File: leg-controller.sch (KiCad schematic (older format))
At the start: 24 parts

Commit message: Added values to some components
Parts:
- removed U?: ATmega328P-PU, Package_DIP:DIP-28_W7.62mm, symbol MCU_Microchip_ATmega:ATmega328P-PU
- added U?: ATmega328P-PU, Package_DIP:DIP-28_W7.62mm, symbol MCU_Microchip_ATmega:ATmega328P-PU
- C?: value C -> 100n
- C? (x2): value C -> 22p
- Y?: value Crystal -> 16MHz
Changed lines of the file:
@@
 	7050 1800 7150 1800
-$Comp
-L MCU_Microchip_ATmega:ATmega328P-PU U?
-U 1 1 618BE8FD
-P 4550 4700
-F 0 "U?" H 3906 4746 50  0000 R CNN
-F 1 "ATmega328P-PU" H 3906 4655 50  0000 R CNN
-F 2 "Package_DIP:DIP-28_W7.62mm" H 4550 4700 50  0001 C CIN
-F 3 "http://ww1.microchip.com/downloads/en/DeviceDoc/ATmega328_P%20AVR%20MCU%20with%20picoPower%20Technology%20Data%20Sheet%2040001984A.pdf" H 4550 4700 50  0001 C CNN
-	1    4550 4700
-	1    0    0    -1
-$EndComp
 $Comp
 L power:+3.3V #PWR?
@@
 P 3850 6400
 F 0 "C?" H 3965 6446 50  0000 L CNN
-F 1 "C" H 3965 6355 50  0000 L CNN
+F 1 "100n" H 3965 6355 50  0000 L CNN
 F 2 "" H 3888 6250 50  0001 C CNN
 F 3 "~" H 3850 6400 50  0001 C CNN
@@
 P 5550 6150
 F 0 "Y?" H 5550 5882 50  0000 C CNN
-F 1 "Crystal" H 5550 5973 50  0000 C CNN
+F 1 "16MHz" H 5550 5973 50  0000 C CNN
 F 2 "" H 5550 6150 50  0001 C CNN
 F 3 "~" H 5550 6150 50  0001 C CNN
@@
 P 5350 6400
 F 0 "C?" H 5465 6446 50  0000 L CNN
-F 1 "C" H 5465 6355 50  0000 L CNN
+F 1 "22p" H 5465 6355 50  0000 L CNN
 F 2 "" H 5388 6250 50  0001 C CNN
 F 3 "~" H 5350 6400 50  0001 C CNN
@@
 P 5750 6400
 F 0 "C?" H 5865 6446 50  0000 L CNN
-F 1 "C" H 5865 6355 50  0000 L CNN
+F 1 "22p" H 5865 6355 50  0000 L CNN
 F 2 "" H 5788 6250 50  0001 C CNN
 F 3 "~" H 5750 6400 50  0001 C CNN
@@
 Wire Wire Line
 	5900 4600 5150 4600
+$Comp
+L MCU_Microchip_ATmega:ATmega328P-PU U?
+U 1 1 617FB84E
+P 4550 4700
+F 0 "U?" H 3906 4746 50  0000 R CNN
+F 1 "ATmega328P-PU" H 3906 4655 50  0000 R CNN
+F 2 "Package_DIP:DIP-28_W7.62mm" H 4550 4700 50  0001 C CIN
+F 3 "http://ww1.microchip.com/downloads/en/DeviceDoc/ATmega328_P%20AVR%20MCU%20with%20picoPower%20Technology%20Data%20Sheet%2040001984A.pdf" H 4550 4700 50  0001 C CNN
+	1    4550 4700
+	1    0    0    -1
+$EndComp
 $EndSCHEMATC

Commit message: Various changes.
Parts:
- removed C?: C, symbol Device:C
- removed D?: D_Zener, symbol Device:D_Zener
- removed J? (x2): Conn_01x03, symbol Connector_Generic:Conn_01x03
- removed J?: Conn_02x01, symbol Connector_Generic:Conn_02x01
- removed Q?: Q_NPN_BCE, symbol Device:Q_NPN_BCE
- removed Q?: Q_PMOS_DGS, symbol Device:Q_PMOS_DGS
- removed R? (x9): R, symbol Device:R
- removed U?: Opamp_Quad_Generic, symbol Device:Opamp_Quad_Generic
- removed U?: ATmega328P-PU, Package_DIP:DIP-28_W7.62mm, symbol MCU_Microchip_ATmega:ATmega328P-PU
- added C1: 470u, symbol Device:C
- added C? (x2): CP, symbol Device:CP
- added J1: Conn_01x02, symbol Connector_Generic:Conn_01x02
- added R1: 0, symbol Device:R
- added U1: ATmega644P-20AU, Package_QFP:TQFP-44_10x10mm_P0.8mm, symbol MCU_Microchip_ATmega:ATmega644P-20AU
- added U?: LD1117S33TR_SOT223, Package_TO_SOT_SMD:SOT-223-3_TabPin2, symbol Regulator_Linear:LD1117S33TR_SOT223
- Y1: renamed from Y?; value 16MHz -> 12MHz
- gave numbers to parts that had none: 5
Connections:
- net labels added: I2C_SCL, I2C_SDA, ROT_CLK_A, ROT_CLK_B, ROT_CLK_C, ROT_DAT_A, ROT_DAT_B, ROT_DAT_C, SPI_MISO, SPI_MOSI, SPI_SCK
- net labels removed: +BATT, MOTOR_A_DISCONNECT, SCL, SDA
- wire segments 80 -> 68
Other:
- moved on the sheet: C2, C3, C4, Y1

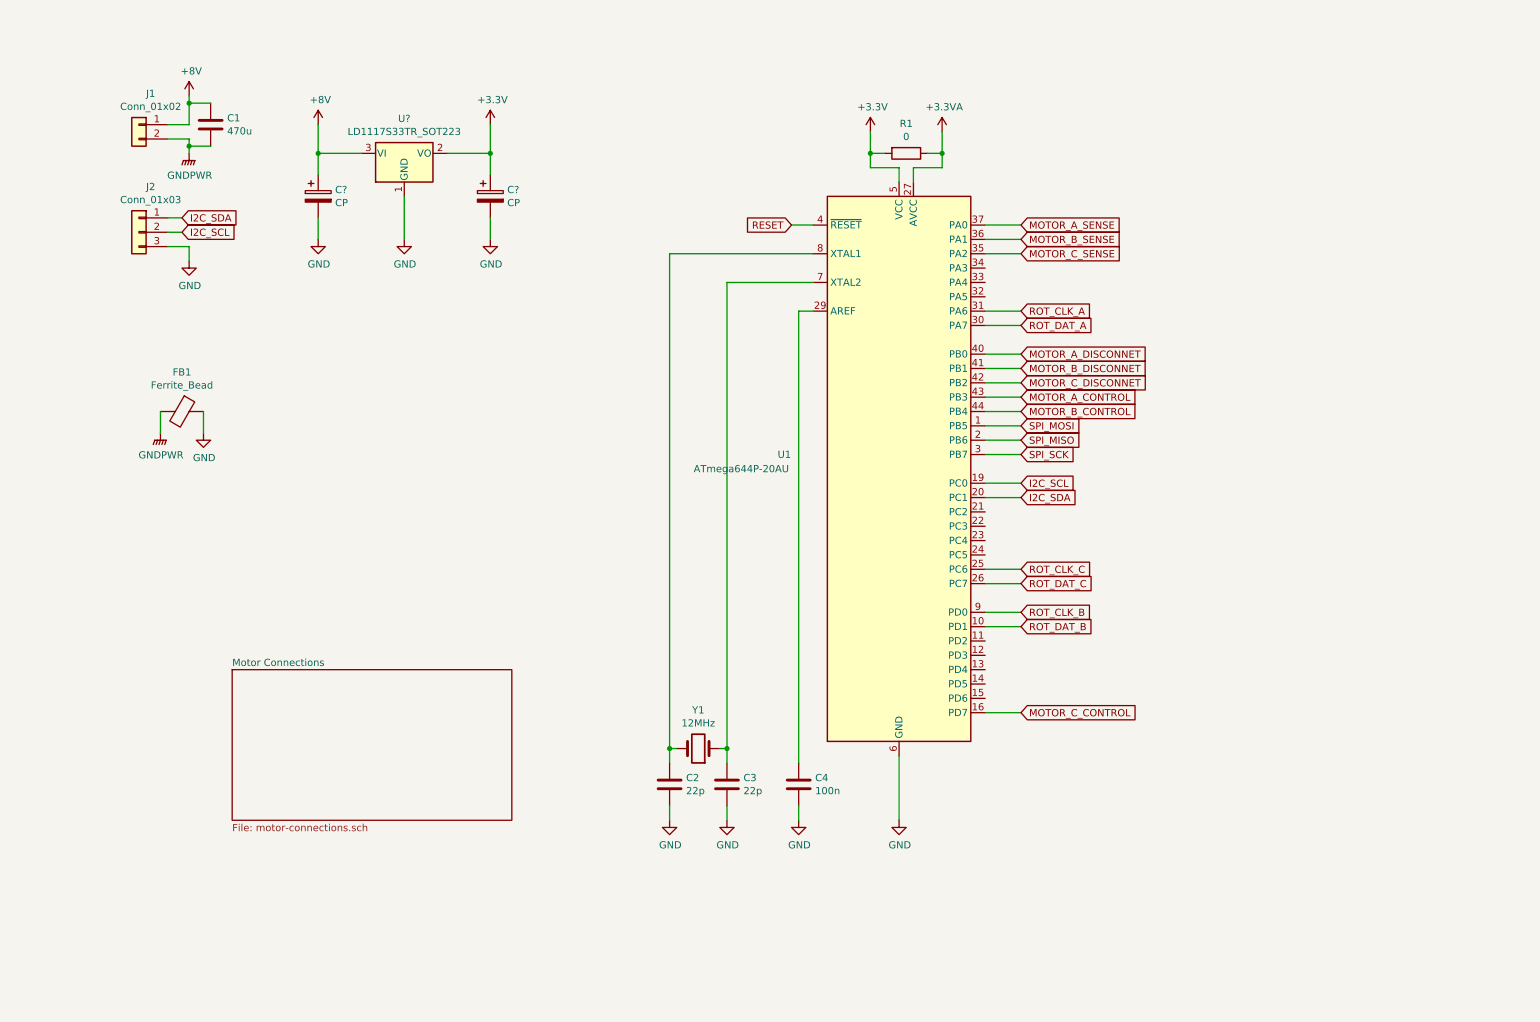
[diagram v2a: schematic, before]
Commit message: Fixed amplifier circuit and did some rearranging
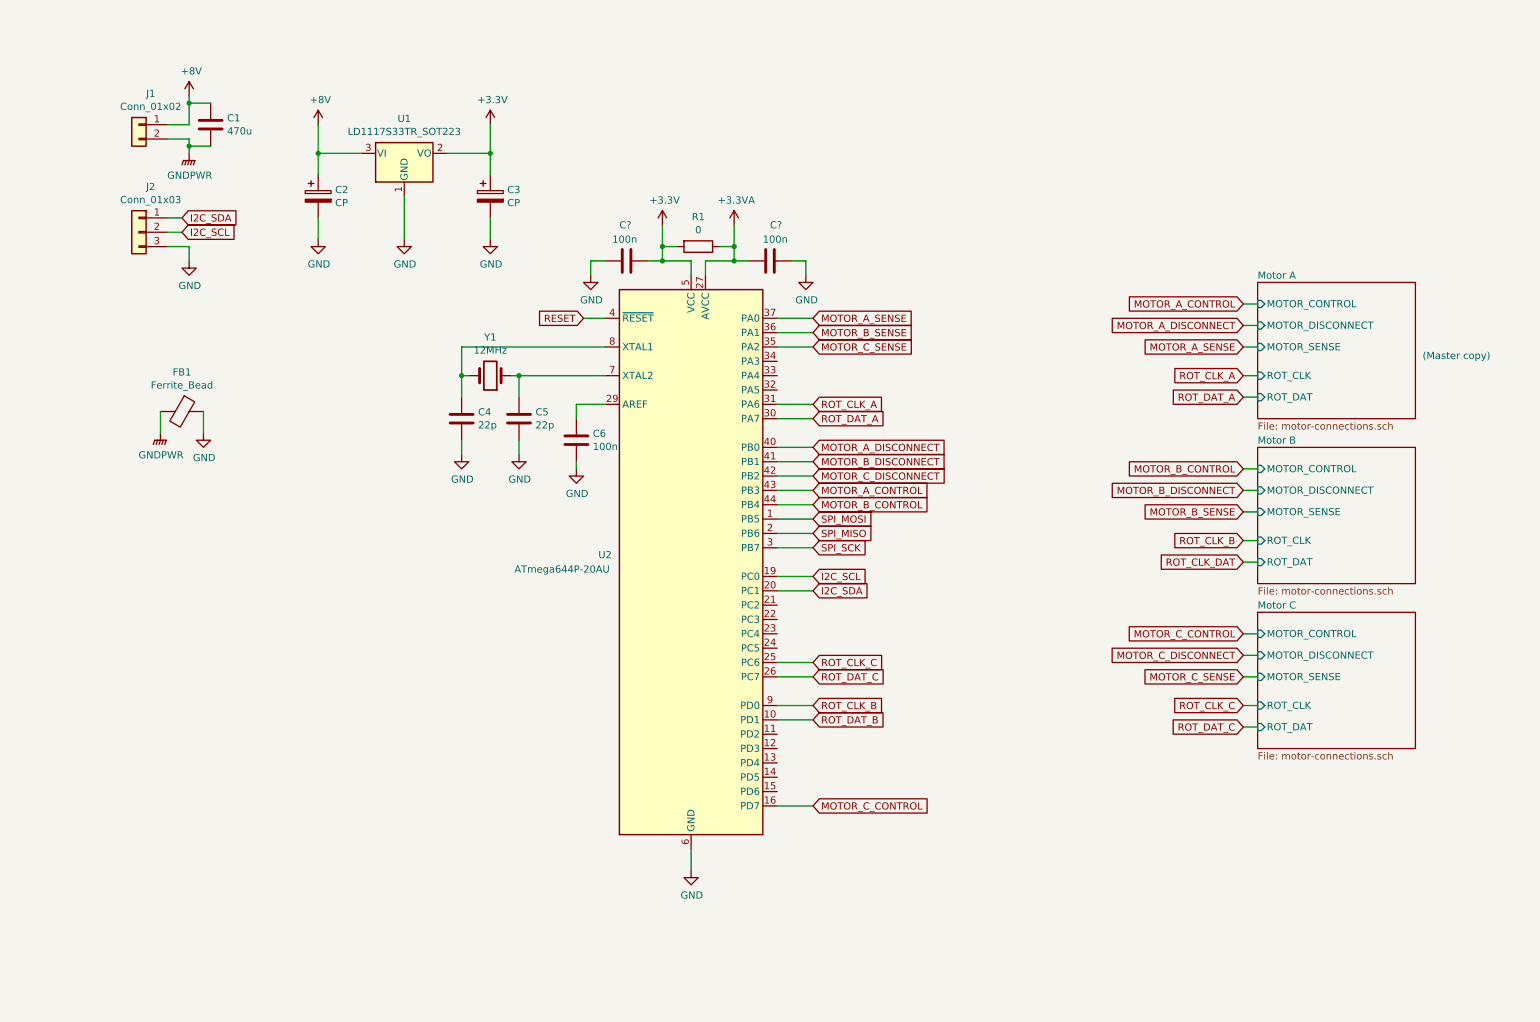
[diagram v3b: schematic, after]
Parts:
- added C? (x2): 100n, symbol Device:C
- gave numbers to parts that had none: 3
- renumbered C2 to C4, C3 to C5, C4 to C6, U1 to U2
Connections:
- net +3.3VA: now also C?.2
- net +3V3: now also C?.1
- net GND: now also C?.1, C?.2
- net MOTOR_A_DISCONNET renamed MOTOR_A_DISCONNECT
- net MOTOR_B_DISCONNET renamed MOTOR_B_DISCONNECT
- net MOTOR_C_DISCONNET renamed MOTOR_C_DISCONNECT
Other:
- note added: "(Master copy)"
- moved on the sheet: C4, C5, C6, R1, U2, Y1

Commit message: Various changes
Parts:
- added D?: LED_RUN, symbol Device:LED
- added D?: LED_POWER, symbol Device:LED
- added D?: LED_3V3, symbol Device:LED
- added D?: LED_ERR, symbol Device:LED
- added D?: D, symbol Device:D
- added J?: Motor_D, symbol Connector_Generic:Conn_01x05
- added J?: Motor_F, symbol Connector_Generic:Conn_01x05
- added J?: Motor_E, symbol Connector_Generic:Conn_01x05
- added J?: ISP, symbol Connector_Generic:Conn_02x03_Odd_Even
- added J?: UART, symbol Connector_Generic:Conn_01x04
- added J?: General_Pins, symbol Connector_Generic:Conn_01x04
- added J?: USB_B_Mini, symbol Connector:USB_B_Mini
- added R? (x4): R, symbol Device:R
- added R? (x2): 68, symbol Device:R
- added R?: 1.5k, symbol Device:R
- J1: value Conn_01x02 -> Power
- J2: value Conn_01x03 -> I2C
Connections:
- net +3V3: now also J?.1 (Pin_1), J?.2 (Pin_2), R?.1, R?.1
- net +8V: now also D?.1 (K), R?.1
- net GND: now also D?.1 (K), D?.1 (K), D?.1 (K), D?.1 (K), J?.4 (Pin_4), J?.4 (Pin_4), J?.5 (GND), J?.5 (Pin_5), J?.5 (Pin_5), J?.5 (Pin_5), J?.6 (Pin_6)
- net MOTOR_A_CONTROL: now also U2.44 (PB4); no longer U2.43 (PB3)
- net MOTOR_A_DISCONNECT: now also U2.21 (PC2); no longer U2.40 (PB0)
- net MOTOR_B_CONTROL: now also U2.15 (PD6); no longer U2.44 (PB4)
- net MOTOR_B_DISCONNECT: now also U2.22 (PC3); no longer U2.41 (PB1)
- net MOTOR_C_DISCONNECT: now also U2.23 (PC4); no longer U2.42 (PB2)
- net RESET: now also J?.5 (Pin_5)
- net SPI_MISO: now also J?.1 (Pin_1), J?.2 (Pin_2), J?.2 (Pin_2), J?.2 (Pin_2)
- net SPI_MOSI: now also J?.1 (Pin_1), J?.1 (Pin_1), J?.1 (Pin_1), J?.4 (Pin_4)
- net SPI_SCK: now also J?.3 (Pin_3), J?.3 (Pin_3), J?.3 (Pin_3), J?.3 (Pin_3)
- net UART_RXD: now reaches U2.11 (PD2)
- net UART_RXD: now also J?.3 (Pin_3)
- net UART_TXD: now reaches U2.12 (PD3)
- net UART_TXD: now also J?.2 (Pin_2)
- net SPI_SS_E: now reaches U2.13 (PD4)
- net SPI_SS_E: now also J?.4 (Pin_4)
- net SPI_SS_F: now reaches U2.14 (PD5)
- net SPI_SS_F: now also J?.4 (Pin_4)
- net SPI_SS_D: now reaches U2.24 (PC5)
- net SPI_SS_D: now also J?.4 (Pin_4)
- net GENERAL_C: now reaches U2.32 (PA5)
- net GENERAL_C: now also J?.3 (Pin_3)
- net GENERAL_B: now reaches U2.33 (PA4)
- net GENERAL_B: now also J?.2 (Pin_2)
- net GENERAL_A: now reaches U2.34 (PA3)
- net GENERAL_A: now also J?.1 (Pin_1)
- new net: D?.2 (A), R?.2 (x4)
- new net: J?.2 (D-), R?.1, R?.2
- new net: J?.3 (D+), R?.2
- new net +5V: D?.2 (A), J?.1 (VBUS)
- new net LED_ERR: R?.1, U2.41 (PB1)
- new net LED_RUN: R?.1, U2.40 (PB0)
- new net USB_D+: R?.1, U2.42 (PB2)
- new net USB_D-: R?.2, U2.43 (PB3)
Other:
- moved on the sheet: C1, C2, C3, C4, C5, C6, C?, FB1, J1, J2, R1, U1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

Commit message: Various changes.
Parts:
- removed J?: General_Pins, symbol Connector_Generic:Conn_01x04
- added SW?: Function, symbol Switch:SW_DIP_x04
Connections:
- net GND: now also SW?.5, SW?.6, SW?.7, SW?.8
- net GENERAL_A renamed FUNCTION_0
- net FUNCTION_0: now also SW?.1
- net GENERAL_B renamed FUNCTION_1
- net FUNCTION_1: now also SW?.2
- net GENERAL_C renamed FUNCTION_2
- net FUNCTION_2: now also SW?.3
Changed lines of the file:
@@
 Wire Wire Line
 	3150 3250 3250 3250
-Text GLabel 1150 4050 2    50   Input ~ 0
-GENERAL_A
-Text GLabel 1150 4150 2    50   Input ~ 0
-GENERAL_B
-Text GLabel 1150 4250 2    50   Input ~ 0
-GENERAL_C
-Wire Wire Line
-	1150 4050 1050 4050
-Wire Wire Line
-	1050 4150 1150 4150
-Wire Wire Line
-	1150 4250 1050 4250
-$Comp
-L power:GND #PWR?
-U 1 1 61C68C47
-P 1150 4450
-F 0 "#PWR?" H 1150 4200 50  0001 C CNN
-F 1 "GND" H 1155 4277 50  0000 C CNN
-F 2 "" H 1150 4450 50  0001 C CNN
-F 3 "" H 1150 4450 50  0001 C CNN
-	1    1150 4450
-	-1   0    0    -1
-$EndComp
-Wire Wire Line
-	1150 4450 1150 4350
-Wire Wire Line
-	1150 4350 1050 4350
 $Comp
 L power:+5V #PWR?
@@
 $Comp
 L Connector_Generic:Conn_01x04 J?
-U 1 1 61C5169E
-P 850 4150
-F 0 "J?" H 768 4467 50  0000 C CNN
-F 1 "General_Pins" H 768 4376 50  0000 C CNN
-F 2 "" H 850 4150 50  0001 C CNN
-F 3 "~" H 850 4150 50  0001 C CNN
-	1    850  4150
-	-1   0    0    -1
-$EndComp
-$Comp
-L power:GND #PWR04
-U 1 1 6179673C
-P 1200 5300
-F 0 "#PWR04" H 1200 5050 50  0001 C CNN
-F 1 "GND" H 1205 5127 50  0000 C CNN
-F 2 "" H 1200 5300 50  0001 C CNN
-F 3 "" H 1200 5300 50  0001 C CNN
-	1    1200 5300
-	1    0    0    -1
-$EndComp
-Wire Wire Line
-	1200 5200 1200 5300
-Wire Wire Line
-	1050 5200 1200 5200
-Wire Wire Line
-	1050 5000 1150 5000
-Wire Wire Line
-	1050 5100 1150 5100
-Text GLabel 1150 5000 2    50   Input ~ 0
-I2C_SDA
-Text GLabel 1150 5100 2    50   Input ~ 0
-I2C_SCL
-$Comp
-L Connector_Generic:Conn_01x03 J2
-U 1 1 61793AA3
-P 850 5100
-F 0 "J2" H 768 5417 50  0000 C CNN
-F 1 "I2C" H 768 5326 50  0000 C CNN
-F 2 "" H 850 5100 50  0001 C CNN
-F 3 "~" H 850 5100 50  0001 C CNN
-	1    850  5100
-	-1   0    0    -1
-$EndComp
-$Comp
-L Connector_Generic:Conn_01x04 J?
 U 1 1 61B3D105
 P 850 3200
@@
 Wire Wire Line
 	1050 3200 1150 3200
-$Comp
-L Connector:USB_B_Mini J?
-U 1 1 61C85C74
-P 2450 4800
-F 0 "J?" H 2507 5267 50  0000 C CNN
-F 1 "USB_B_Mini" H 2507 5176 50  0000 C CNN
-F 2 "" H 2600 4750 50  0001 C CNN
-F 3 "~" H 2600 4750 50  0001 C CNN
-	1    2450 4800
-	1    0    0    -1
-$EndComp
-$Comp
-L Device:R R?
-U 1 1 61C9C39E
-P 3350 4800
-F 0 "R?" V 3143 4800 50  0000 C CNN
-F 1 "68" V 3234 4800 50  0000 C CNN
-F 2 "" V 3280 4800 50  0001 C CNN
-F 3 "~" H 3350 4800 50  0001 C CNN
-	1    3350 4800
-	0    1    1    0
-$EndComp
-$Comp
-L Device:R R?
-U 1 1 61C9D08A
-P 3350 4900
-F 0 "R?" V 3250 4900 50  0000 C CNN
-F 1 "68" V 3150 4900 50  0000 C CNN
-F 2 "" V 3280 4900 50  0001 C CNN
-F 3 "~" H 3350 4900 50  0001 C CNN
-	1    3350 4900
-	0    -1   -1   0
-$EndComp
-$Comp
-L Device:R R?
-U 1 1 61CB53AC
-P 3100 4400
-F 0 "R?" H 3170 4446 50  0000 L CNN
-F 1 "1.5k" H 3170 4355 50  0000 L CNN
-F 2 "" V 3030 4400 50  0001 C CNN
-F 3 "~" H 3100 4400 50  0001 C CNN
-	1    3100 4400
-	1    0    0    -1
-$EndComp
-Wire Wire Line
-	3100 4550 3100 4900
-Connection ~ 3100 4900
-Wire Wire Line
-	3100 4900 3200 4900
-$Comp
-L power:+3.3V #PWR?
-U 1 1 61CBCED0
-P 3100 4150
-F 0 "#PWR?" H 3100 4000 50  0001 C CNN
-F 1 "+3.3V" H 3115 4323 50  0000 C CNN
-F 2 "" H 3100 4150 50  0001 C CNN
-F 3 "" H 3100 4150 50  0001 C CNN
-	1    3100 4150
-	1    0    0    -1
-$EndComp
-Wire Wire Line
-	3100 4150 3100 4250
-$Comp
-L power:GND #PWR?
-U 1 1 61CC49B7
-P 2450 5300
-F 0 "#PWR?" H 2450 5050 50  0001 C CNN
-F 1 "GND" H 2455 5127 50  0000 C CNN
-F 2 "" H 2450 5300 50  0001 C CNN
-F 3 "" H 2450 5300 50  0001 C CNN
-	1    2450 5300
-	1    0    0    -1
-$EndComp
-Wire Wire Line
-	2450 5200 2450 5300
-Wire Wire Line
-	3600 4800 3500 4800
-Wire Wire Line
-	3500 4900 3600 4900
-$Comp
-L power:+5V #PWR?
-U 1 1 61D1E6C0
-P 2850 4150
-F 0 "#PWR?" H 2850 4000 50  0001 C CNN
-F 1 "+5V" H 2865 4323 50  0000 C CNN
-F 2 "" H 2850 4150 50  0001 C CNN
-F 3 "" H 2850 4150 50  0001 C CNN
-	1    2850 4150
-	1    0    0    -1
-$EndComp
-Wire Wire Line
-	2750 4600 2850 4600
-Wire Wire Line
-	2850 4600 2850 4150
-Wire Wire Line
-	2750 4800 3200 4800
-Wire Wire Line
-	2750 4900 3100 4900
 Wire Wire Line
 	3550 6200 3450 6200
@@
 	6500 5200 6750 5200
 Text GLabel 6750 2600 2    50   Input ~ 0
-GENERAL_A
+FUNCTION_0
 Text GLabel 6750 2700 2    50   Input ~ 0
-GENERAL_B
+FUNCTION_1
 Text GLabel 6750 2800 2    50   Input ~ 0
-GENERAL_C
+FUNCTION_2
 Wire Wire Line
 	6750 2600 6500 2600
@@
 Wire Wire Line
 	4700 2700 5300 2700
+Text GLabel 3600 4800 2    50   Input ~ 0
+USB_D+
 Text GLabel 3600 4900 2    50   Input ~ 0
 USB_D-
-Text GLabel 3600 4800 2    50   Input ~ 0
-USB_D+
+Wire Wire Line
+	2750 4900 3100 4900
+Wire Wire Line
+	2750 4800 3200 4800
+Wire Wire Line
+	2850 4600 2850 4150
+Wire Wire Line
+	2750 4600 2850 4600
+$Comp
+L power:+5V #PWR?
+U 1 1 61D1E6C0
+P 2850 4150
+F 0 "#PWR?" H 2850 4000 50  0001 C CNN
+F 1 "+5V" H 2865 4323 50  0000 C CNN
+F 2 "" H 2850 4150 50  0001 C CNN
+F 3 "" H 2850 4150 50  0001 C CNN
+	1    2850 4150
+	1    0    0    -1
+$EndComp
+Wire Wire Line
+	3500 4900 3600 4900
+Wire Wire Line
+	3600 4800 3500 4800
+Wire Wire Line
+	2450 5200 2450 5300
+$Comp
+L power:GND #PWR?
+U 1 1 61CC49B7
+P 2450 5300
+F 0 "#PWR?" H 2450 5050 50  0001 C CNN
+F 1 "GND" H 2455 5127 50  0000 C CNN
+F 2 "" H 2450 5300 50  0001 C CNN
+F 3 "" H 2450 5300 50  0001 C CNN
+	1    2450 5300
+	1    0    0    -1
+$EndComp
+Wire Wire Line
+	3100 4150 3100 4250
+$Comp
+L power:+3.3V #PWR?
+U 1 1 61CBCED0
+P 3100 4150
+F 0 "#PWR?" H 3100 4000 50  0001 C CNN
+F 1 "+3.3V" H 3115 4323 50  0000 C CNN
+F 2 "" H 3100 4150 50  0001 C CNN
+F 3 "" H 3100 4150 50  0001 C CNN
+	1    3100 4150
+	1    0    0    -1
+$EndComp
+Wire Wire Line
+	3100 4900 3200 4900
+Connection ~ 3100 4900
+Wire Wire Line
+	3100 4550 3100 4900
+$Comp
+L Device:R R?
+U 1 1 61CB53AC
+P 3100 4400
+F 0 "R?" H 3170 4446 50  0000 L CNN
+F 1 "1.5k" H 3170 4355 50  0000 L CNN
+F 2 "" V 3030 4400 50  0001 C CNN
+F 3 "~" H 3100 4400 50  0001 C CNN
+	1    3100 4400
+	1    0    0    -1
+$EndComp
+$Comp
+L Device:R R?
+U 1 1 61C9D08A
+P 3350 4900
+F 0 "R?" V 3250 4900 50  0000 C CNN
+F 1 "68" V 3150 4900 50  0000 C CNN
+F 2 "" V 3280 4900 50  0001 C CNN
+F 3 "~" H 3350 4900 50  0001 C CNN
+	1    3350 4900
+	0    -1   -1   0
+$EndComp
+$Comp
+L Device:R R?
+U 1 1 61C9C39E
+P 3350 4800
+F 0 "R?" V 3143 4800 50  0000 C CNN
+F 1 "68" V 3234 4800 50  0000 C CNN
+F 2 "" V 3280 4800 50  0001 C CNN
+F 3 "~" H 3350 4800 50  0001 C CNN
+	1    3350 4800
+	0    1    1    0
+$EndComp
+$Comp
+L Connector:USB_B_Mini J?
+U 1 1 61C85C74
+P 2450 4800
+F 0 "J?" H 2507 5267 50  0000 C CNN
+F 1 "USB_B_Mini" H 2507 5176 50  0000 C CNN
+F 2 "" H 2600 4750 50  0001 C CNN
+F 3 "~" H 2600 4750 50  0001 C CNN
+	1    2450 4800
+	1    0    0    -1
+$EndComp
+$Comp
+L Connector_Generic:Conn_01x03 J2
+U 1 1 61793AA3
+P 850 5100
+F 0 "J2" H 768 5417 50  0000 C CNN
+F 1 "I2C" H 768 5326 50  0000 C CNN
+F 2 "" H 850 5100 50  0001 C CNN
+F 3 "~" H 850 5100 50  0001 C CNN
+	1    850  5100
+	-1   0    0    -1
+$EndComp
+Text GLabel 1150 5100 2    50   Input ~ 0
+I2C_SCL
+Text GLabel 1150 5000 2    50   Input ~ 0
+I2C_SDA
+Wire Wire Line
+	1050 5100 1150 5100
+Wire Wire Line
+	1050 5000 1150 5000
+Wire Wire Line
+	1050 5200 1200 5200
+Wire Wire Line
+	1200 5200 1200 5300
+$Comp
+L power:GND #PWR04
+U 1 1 6179673C
+P 1200 5300
+F 0 "#PWR04" H 1200 5050 50  0001 C CNN
+F 1 "GND" H 1205 5127 50  0000 C CNN
+F 2 "" H 1200 5300 50  0001 C CNN
+F 3 "" H 1200 5300 50  0001 C CNN
+	1    1200 5300
+	1    0    0    -1
+$EndComp
+Wire Wire Line
+	1200 4300 1300 4300
+Wire Wire Line
+	1200 4200 1300 4200
+Wire Wire Line
+	1200 4100 1300 4100
+Text GLabel 1200 4300 0    50   Input ~ 0
+FUNCTION_2
+Text GLabel 1200 4200 0    50   Input ~ 0
+FUNCTION_1
+Text GLabel 1200 4100 0    50   Input ~ 0
+FUNCTION_0
+Wire Wire Line
+	2000 4400 2000 4500
+Connection ~ 2000 4400
+Wire Wire Line
+	1900 4400 2000 4400
+Wire Wire Line
+	2000 4300 2000 4400
+Connection ~ 2000 4300
+Wire Wire Line
+	1900 4300 2000 4300
+Wire Wire Line
+	2000 4200 2000 4300
+Connection ~ 2000 4200
+Wire Wire Line
+	1900 4200 2000 4200
+Wire Wire Line
+	2000 4100 2000 4200
+Wire Wire Line
+	1900 4100 2000 4100
+$Comp
+L power:GND #PWR?
+U 1 1 6199B184
+P 2000 4500
+F 0 "#PWR?" H 2000 4250 50  0001 C CNN
+F 1 "GND" H 2005 4327 50  0000 C CNN
+F 2 "" H 2000 4500 50  0001 C CNN
+F 3 "" H 2000 4500 50  0001 C CNN
+	1    2000 4500
+	1    0    0    -1
+$EndComp
+$Comp
+L Switch:SW_DIP_x04 SW?
+U 1 1 6199597A
+P 1600 4300
+F 0 "SW?" H 1600 4767 50  0000 C CNN
+F 1 "Function" H 1600 4676 50  0000 C CNN
+F 2 "" H 1600 4300 50  0001 C CNN
+F 3 "~" H 1600 4300 50  0001 C CNN
+	1    1600 4300
+	1    0    0    -1
+$EndComp
 $EndSCHEMATC

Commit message: Assigned footprints
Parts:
- C10, C11: renamed from C?; footprint (none) -> Capacitor_SMD:C_0603_1608Metric_Pad1.05x0.95mm_HandSolder
- C4, C5, C6: footprint (none) -> Capacitor_SMD:C_0603_1608Metric_Pad1.05x0.95mm_HandSolder
- D4, D5, D7, D8: renamed from D?; footprint (none) -> LED_SMD:LED_0603_1608Metric_Pad1.05x0.95mm_HandSolder
- J1: footprint (none) -> TerminalBlock:TerminalBlock_Altech_AK300-2_P5.00mm
- R1: footprint (none) -> Resistor_SMD:R_0603_1608Metric_Pad1.05x0.95mm_HandSolder
- R35, R36, R37, R38, R39, R40, R41: renamed from R?; footprint (none) -> Resistor_SMD:R_0603_1608Metric_Pad1.05x0.95mm_HandSolder
- gave numbers to parts that had none: 8
